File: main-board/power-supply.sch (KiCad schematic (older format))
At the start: 18 parts

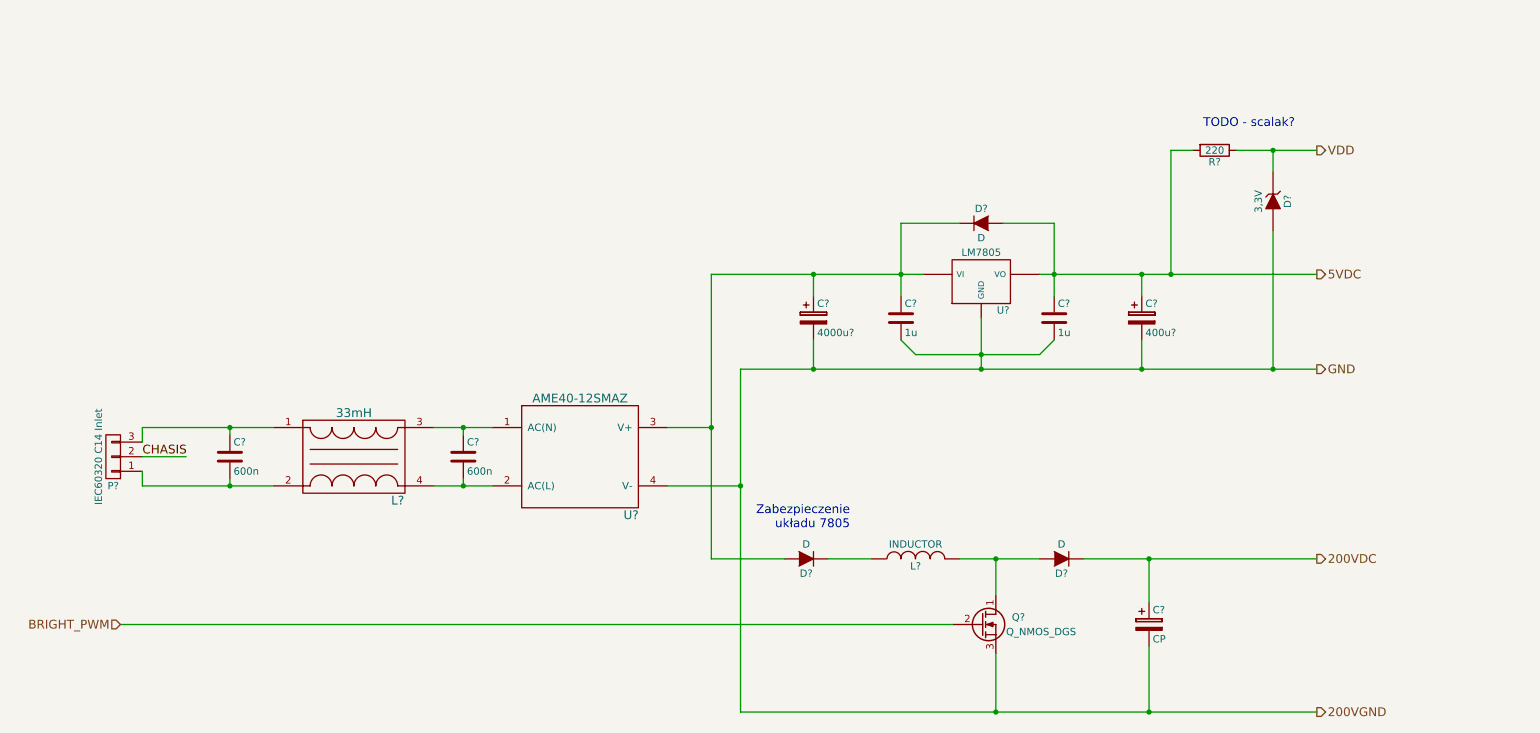
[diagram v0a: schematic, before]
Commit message: GPIO Expander - podlaczenie do STM32; wyprowadzenia dla modulow NIXIE; zasilanie - do poprawki (GPIO Expander zasilany z 5V - STM 3,3V
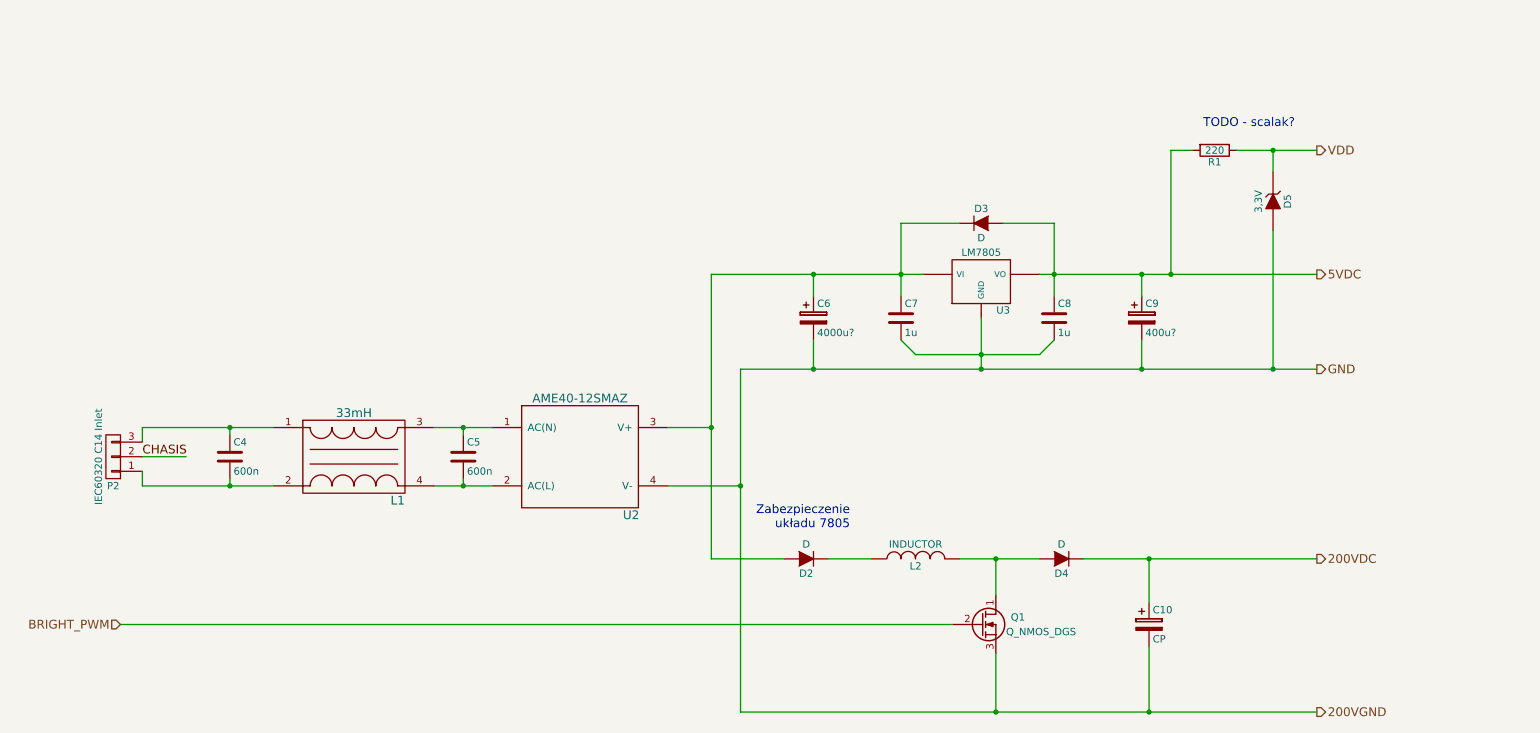
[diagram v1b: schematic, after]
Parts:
- gave numbers to parts that had none: 18
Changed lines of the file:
@@
 $Descr A4 11693 8268
 encoding utf-8
-Sheet 2 2
+Sheet 2 4
 Title "Nixie clock power supply"
 Date ""
@@
 $EndDescr
 $Comp
-L AME40-12SMAZ U?
+L AME40-12SMAZ U2
 U 1 1 5814F918
 P 4400 3700
-F 0 "U?" H 4750 3300 60  0000 C CNN
+F 0 "U2" H 4750 3300 60  0000 C CNN
 F 1 "AME40-12SMAZ" H 4400 4100 60  0000 C CNN
 F 2 "" H 4400 3700 60  0001 C CNN
@@
 $EndComp
 $Comp
-L C C?
+L C C5
 U 1 1 5814FA42
 P 3600 3700
-F 0 "C?" H 3625 3800 50  0000 L CNN
+F 0 "C5" H 3625 3800 50  0000 L CNN
 F 1 "600n" H 3625 3600 50  0000 L CNN
 F 2 "" H 3638 3550 50  0000 C CNN
@@
 $EndComp
 $Comp
-L DTSN-12/33/0.9 L?
+L DTSN-12/33/0.9 L1
 U 1 1 58150127
 P 2850 3700
-F 0 "L?" H 3150 3400 60  0000 C CNN
+F 0 "L1" H 3150 3400 60  0000 C CNN
 F 1 "33mH" H 2850 4000 60  0000 C CNN
 F 2 "" H 2800 3900 60  0001 C CNN
@@
 Connection ~ 3600 3500
 $Comp
-L C C?
+L C C4
 U 1 1 58150356
 P 2000 3700
-F 0 "C?" H 2025 3800 50  0000 L CNN
+F 0 "C4" H 2025 3800 50  0000 L CNN
 F 1 "600n" H 2025 3600 50  0000 L CNN
 F 2 "" H 2038 3550 50  0000 C CNN
@@
 $EndComp
 $Comp
-L CONN_01X03 P?
+L CONN_01X03 P2
 U 1 1 581505F1
 P 1200 3700
-F 0 "P?" H 1200 3900 50  0000 C CNN
+F 0 "P2" H 1200 3900 50  0000 C CNN
 F 1 "IEC60320 C14 Inlet" V 1300 3700 50  0000 C CNN
 F 2 "" H 1200 3700 50  0000 C CNN
@@
 	5000 3900 5500 3900
 $Comp
-L LM7805 U?
+L LM7805 U3
 U 1 1 581516AA
 P 7150 2500
-F 0 "U?" H 7300 2304 50  0000 C CNN
+F 0 "U3" H 7300 2304 50  0000 C CNN
 F 1 "LM7805" H 7150 2700 50  0000 C CNN
 F 2 "" H 7150 2500 50  0000 C CNN
@@
 $EndComp
 $Comp
-L CP C?
+L CP C6
 U 1 1 58151831
 P 6000 2750
-F 0 "C?" H 6025 2850 50  0000 L CNN
+F 0 "C6" H 6025 2850 50  0000 L CNN
 F 1 "4000u?" H 6025 2650 50  0000 L CNN
 F 2 "" H 6038 2600 50  0000 C CNN
@@
 $EndComp
 $Comp
-L CP C?
+L CP C9
 U 1 1 581518E5
 P 8250 2750
-F 0 "C?" H 8275 2850 50  0000 L CNN
+F 0 "C9" H 8275 2850 50  0000 L CNN
 F 1 "400u?" H 8275 2650 50  0000 L CNN
 F 2 "" H 8288 2600 50  0000 C CNN
@@
 $EndComp
 $Comp
-L C C?
+L C C7
 U 1 1 58151B4F
 P 6600 2750
-F 0 "C?" H 6625 2850 50  0000 L CNN
+F 0 "C7" H 6625 2850 50  0000 L CNN
 F 1 "1u" H 6625 2650 50  0000 L CNN
 F 2 "" H 6638 2600 50  0000 C CNN
@@
 $EndComp
 $Comp
-L C C?
+L C C8
 U 1 1 58151BB1
 P 7650 2750
-F 0 "C?" H 7675 2850 50  0000 L CNN
+F 0 "C8" H 7675 2850 50  0000 L CNN
 F 1 "1u" H 7675 2650 50  0000 L CNN
 F 2 "" H 7688 2600 50  0000 C CNN
@@
 Connection ~ 6000 3100
 $Comp
-L INDUCTOR L?
+L INDUCTOR L2
 U 1 1 581538C6
 P 6700 4400
-F 0 "L?" V 6650 4400 50  0000 C CNN
+F 0 "L2" V 6650 4400 50  0000 C CNN
 F 1 "INDUCTOR" V 6800 4400 50  0000 C CNN
 F 2 "" H 6700 4400 50  0000 C CNN
@@
 $EndComp
 $Comp
-L D D?
+L D D3
 U 1 1 581539A7
 P 7150 2100
-F 0 "D?" H 7150 2200 50  0000 C CNN
+F 0 "D3" H 7150 2200 50  0000 C CNN
 F 1 "D" H 7150 2000 50  0000 C CNN
 F 2 "" H 7150 2100 50  0000 C CNN
@@
 	7000 2100 6600 2100
 $Comp
-L Q_NMOS_DGS Q?
+L Q_NMOS_DGS Q1
 U 1 1 581540AF
 P 7150 4850
-F 0 "Q?" H 7450 4900 50  0000 R CNN
+F 0 "Q1" H 7450 4900 50  0000 R CNN
 F 1 "Q_NMOS_DGS" H 7800 4800 50  0000 R CNN
 F 2 "" H 7350 4950 50  0000 C CNN
@@
 $EndComp
 $Comp
-L D D?
+L D D4
 U 1 1 58154490
 P 7700 4400
-F 0 "D?" H 7700 4500 50  0000 C CNN
+F 0 "D4" H 7700 4500 50  0000 C CNN
 F 1 "D" H 7700 4300 50  0000 C CNN
 F 2 "" H 7700 4400 50  0000 C CNN
@@
 $EndComp
 $Comp
-L CP C?
+L CP C10
 U 1 1 58154567
 P 8300 4850
-F 0 "C?" H 8325 4950 50  0000 L CNN
+F 0 "C10" H 8325 4950 50  0000 L CNN
 F 1 "CP" H 8325 4750 50  0000 L CNN
 F 2 "" H 8338 4700 50  0000 C CNN
@@
 	1250 4850 6950 4850
 $Comp
-L D D?
+L D D2
 U 1 1 58170BE4
 P 5950 4400
-F 0 "D?" H 5950 4500 50  0000 C CNN
+F 0 "D2" H 5950 4500 50  0000 C CNN
 F 1 "D" H 5950 4300 50  0000 C CNN
 F 2 "" H 5950 4400 50  0000 C CNN
@@
 200VGND
 $Comp
-L ZENER D?
+L ZENER D5
 U 1 1 58179AB5
 P 9150 1950
-F 0 "D?" H 9150 2050 50  0000 C CNN
+F 0 "D5" H 9150 2050 50  0000 C CNN
 F 1 "3,3V" H 9150 1850 50  0000 C CNN
 F 2 "" H 9150 1950 50  0000 C CNN
@@
 $EndComp
 $Comp
-L R R?
+L R R1
 U 1 1 58179BE8
 P 8750 1600
-F 0 "R?" V 8830 1600 50  0000 C CNN
+F 0 "R1" V 8830 1600 50  0000 C CNN
 F 1 "220" V 8750 1600 50  0000 C CNN
 F 2 "" V 8680 1600 50  0000 C CNN

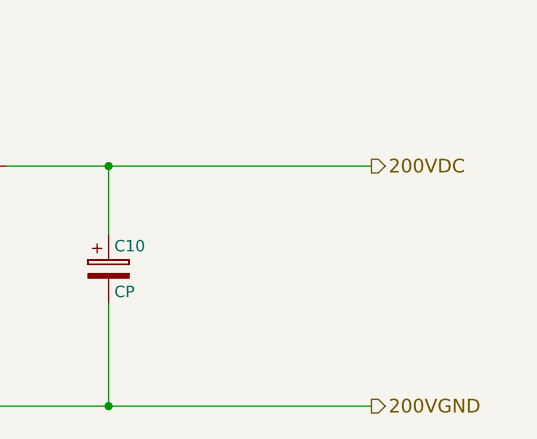
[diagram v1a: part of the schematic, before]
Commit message: #1 - enkoder zamiast potencjometru; pomiar napiecia zarzenia; SWD; BOOT0 do masy
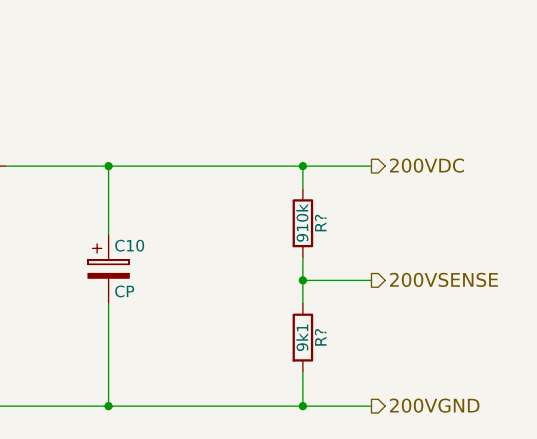
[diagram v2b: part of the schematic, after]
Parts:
- added R?: 910k, symbol R
- added R?: 9k1, symbol R
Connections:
- net 200VDC: now also R?.1
- net 200VGND: now also R?.2
- new net 200VSENSE: R?.1, R?.2
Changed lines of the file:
@@
 LIBS:valves
 LIBS:stm32
+LIBS:sensors
 LIBS:nixie-clock-cache
 EELAYER 25 0
@@
 Text HLabel 1250 4850 0    60   Input ~ 0
 BRIGHT_PWM
+$Comp
+L R R?
+U 1 1 58265B95
+P 9150 4650
+F 0 "R?" V 9230 4650 50  0000 C CNN
+F 1 "910k" V 9150 4650 50  0000 C CNN
+F 2 "" V 9080 4650 50  0000 C CNN
+F 3 "" H 9150 4650 50  0000 C CNN
+	1    9150 4650
+	1    0    0    -1
+$EndComp
+$Comp
+L R R?
+U 1 1 58265EBE
+P 9150 5150
+F 0 "R?" V 9230 5150 50  0000 C CNN
+F 1 "9k1" V 9150 5150 50  0000 C CNN
+F 2 "" V 9080 5150 50  0000 C CNN
+F 3 "" H 9150 5150 50  0000 C CNN
+	1    9150 5150
+	1    0    0    -1
+$EndComp
+Wire Wire Line
+	9150 4400 9150 4500
+Connection ~ 9150 4400
+Wire Wire Line
+	9150 4800 9150 5000
+Wire Wire Line
+	9150 5300 9150 5450
+Connection ~ 9150 5450
+Text HLabel 9450 4900 2    60   Output ~ 0
+200VSENSE
+Wire Wire Line
+	9150 4900 9450 4900
+Connection ~ 9150 4900
 $EndSCHEMATC

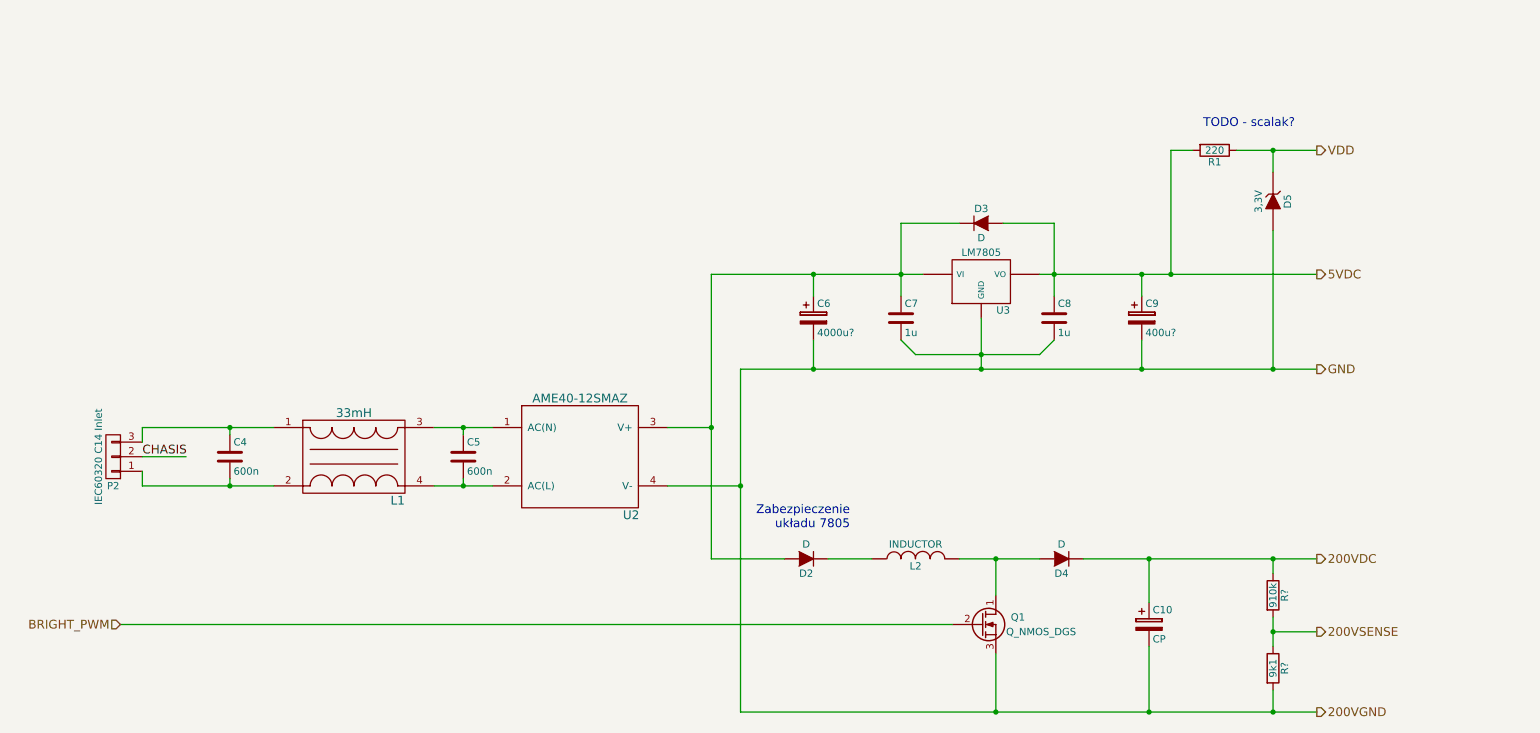
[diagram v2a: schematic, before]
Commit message: #1 - zmiana wartosci kondensator do typuszeregu, usuniecie D2, UF4004 na D4, przyciagniecie do masy bramki Q1, bezpiecznik na wejsciu przetwornicy, gniazdo IEC C7, 100n na zasilaniu PCF8574
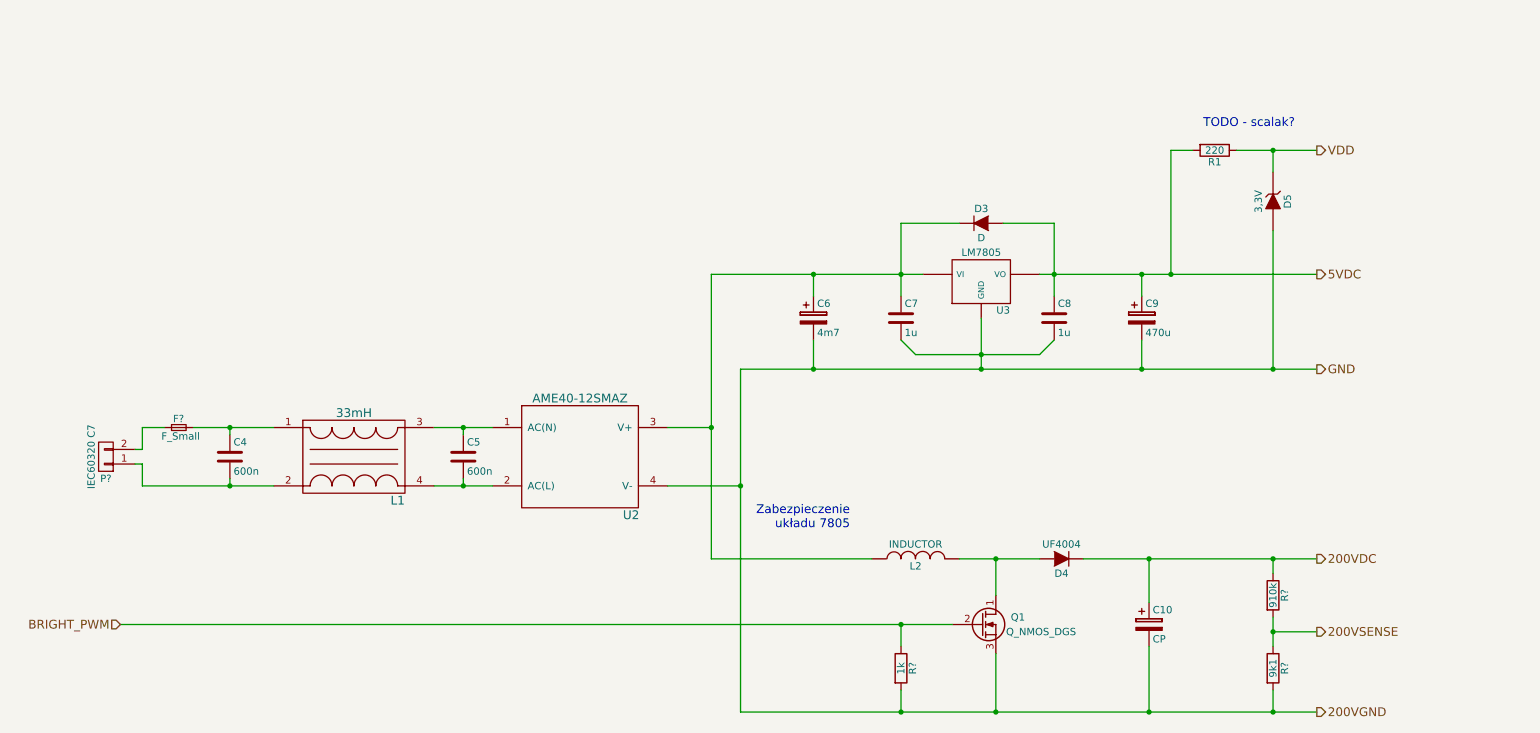
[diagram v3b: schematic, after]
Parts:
- removed D2: D, symbol D
- removed P2: IEC60320 C14 Inlet, symbol CONN_01X03
- added F?: F_Small, symbol F_Small
- added P?: IEC60320 C7, symbol CONN_01X02
- added R?: 1k, symbol R
- C6: value 4000u? -> 4m7
- C9: value 400u? -> 470u
- D4: value D -> UF4004
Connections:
- net 200VGND: now also R?.2
- net BRIGHT_PWM: now also R?.1
- net at C6.1, C7.1, D3.1 (K)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: now also L2.1
- net at C4.1, L1.1: now also F?.2
- net at C4.2, L1.2: now also P?.1 (P1)
- new net: F?.1, P?.2 (P2)
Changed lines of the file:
@@
 	1    0    0    -1
 $EndComp
-$Comp
-L CONN_01X03 P2
-U 1 1 581505F1
-P 1200 3700
-F 0 "P2" H 1200 3900 50  0000 C CNN
-F 1 "IEC60320 C14 Inlet" V 1300 3700 50  0000 C CNN
-F 2 "" H 1200 3700 50  0000 C CNN
-F 3 "" H 1200 3700 50  0000 C CNN
-	1    1200 3700
-	-1   0    0    1
-$EndComp
-Wire Wire Line
-	1400 3600 1400 3600
-Wire Wire Line
-	1400 3600 1400 3500
-Wire Wire Line
-	1400 3500 2300 3500
+Wire Wire Line
+	1750 3500 2300 3500
 Wire Wire Line
 	2000 3500 2000 3550
-Connection ~ 2000 3500
-Wire Wire Line
-	1400 3800 1400 3900
+Wire Wire Line
+	1400 3750 1400 3900
 Wire Wire Line
 	1400 3900 2300 3900
-Wire Wire Line
-	1400 3700 1700 3700
-Text Label 1400 3700 0    60   ~ 0
-CHASIS
 Wire Wire Line
 	2000 3900 2000 3850
@@
 P 6000 2750
 F 0 "C6" H 6025 2850 50  0000 L CNN
-F 1 "4000u?" H 6025 2650 50  0000 L CNN
+F 1 "4m7" H 6025 2650 50  0000 L CNN
 F 2 "" H 6038 2600 50  0000 C CNN
 F 3 "" H 6000 2750 50  0000 C CNN
@@
 P 8250 2750
 F 0 "C9" H 8275 2850 50  0000 L CNN
-F 1 "400u?" H 8275 2650 50  0000 L CNN
+F 1 "470u" H 8275 2650 50  0000 L CNN
 F 2 "" H 8288 2600 50  0000 C CNN
 F 3 "" H 8250 2750 50  0000 C CNN
@@
 P 7700 4400
 F 0 "D4" H 7700 4500 50  0000 C CNN
-F 1 "D" H 7700 4300 50  0000 C CNN
+F 1 "UF4004" H 7700 4300 50  0000 C CNN
 F 2 "" H 7700 4400 50  0000 C CNN
-F 3 "" H 7700 4400 50  0000 C CNN
+F 3 "http://www.vishay.com/docs/88755/uf4001.pdf" H 7700 4400 50  0001 C CNN
 	1    7700 4400
 	-1   0    0    1
@@
 Connection ~ 5300 3500
 Wire Wire Line
-	7250 5050 7250 5450
+	7250 5450 7250 5050
 Wire Wire Line
 	5500 5450 9450 5450
@@
 Wire Wire Line
 	1250 4850 6950 4850
-$Comp
-L D D2
-U 1 1 58170BE4
-P 5950 4400
-F 0 "D2" H 5950 4500 50  0000 C CNN
-F 1 "D" H 5950 4300 50  0000 C CNN
-F 2 "" H 5950 4400 50  0000 C CNN
-F 3 "" H 5950 4400 50  0000 C CNN
-	1    5950 4400
-	-1   0    0    1
-$EndComp
-Wire Wire Line
-	5300 4400 5800 4400
-Wire Wire Line
-	6100 4400 6400 4400
+Wire Wire Line
+	5300 4400 6400 4400
 Text Notes 6250 4200 2    60   ~ 0
 Zabezpieczenie\nukładu 7805
@@
 	9150 4900 9450 4900
 Connection ~ 9150 4900
+$Comp
+L R R?
+U 1 1 582BEA4B
+P 6600 5150
+F 0 "R?" V 6680 5150 50  0000 C CNN
+F 1 "1k" V 6600 5150 50  0000 C CNN
+F 2 "" V 6530 5150 50  0000 C CNN
+F 3 "" H 6600 5150 50  0000 C CNN
+	1    6600 5150
+	1    0    0    -1
+$EndComp
+Wire Wire Line
+	6600 5000 6600 4850
+Connection ~ 6600 4850
+Wire Wire Line
+	6600 5300 6600 5450
+Connection ~ 6600 5450
+$Comp
+L CONN_01X02 P?
+U 1 1 582BF3C0
+P 1150 3700
+F 0 "P?" H 1150 3850 50  0000 C CNN
+F 1 "IEC60320 C7" V 1250 3700 50  0000 C CNN
+F 2 "" H 1150 3700 50  0000 C CNN
+F 3 "" H 1150 3700 50  0000 C CNN
+	1    1150 3700
+	-1   0    0    1
+$EndComp
+Wire Wire Line
+	1350 3750 1400 3750
+$Comp
+L F_Small F?
+U 1 1 582BFFD9
+P 1650 3500
+F 0 "F?" H 1610 3560 50  0000 L CNN
+F 1 "F_Small" H 1530 3440 50  0000 L CNN
+F 2 "" H 1650 3500 50  0000 C CNN
+F 3 "" H 1650 3500 50  0000 C CNN
+	1    1650 3500
+	1    0    0    -1
+$EndComp
+Connection ~ 2000 3500
+Wire Wire Line
+	1550 3500 1400 3500
+Wire Wire Line
+	1400 3500 1400 3650
+Wire Wire Line
+	1400 3650 1350 3650
 $EndSCHEMATC
